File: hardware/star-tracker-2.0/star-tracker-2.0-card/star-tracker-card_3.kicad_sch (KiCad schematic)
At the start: 60 parts, among them J100 DM3BT-DSF-PEJS, U11 TCAN330, U3 EMMC+RESET+5.1-COMPATIBLE-BA, U7 OSD3358-512M-BSM

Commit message: Added IMU
added IMU, and i2c pull up resistors to schematic.
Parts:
- removed TP1, TP2: TEST-POINT3X4, oresat-misc:TestPoint_Pad_D1.0mm, symbol oresat-misc:Test-Point-1mm-round
- added C40: 100n, oresat-passives:0603-C-NOSILK, symbol Device:C_Small
- added C41: 2.2u, oresat-passives:0603-C-NOSILK, symbol Device:C_Small
- added C44: 10n, oresat-passives:0603-C-NOSILK, symbol Device:C_Small
- added R59, R60, R75, R79: 4.7k, oresat-passives:0603-C-NOSILK, symbol Device:R_Small_US
- added U17: ICM-42688-P, oresat-ics:PQFN50P300X250X97-14N, symbol oresat-ics:ICM-42688-P
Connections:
- net 3.3V: now also C40.1, C41.1, C44.1, R59.2, R75.2, R79.2, U17.5 (VDDIO), U17.8 (VDD)
- net GND: now also C40.2, C41.2, C44.2, R60.1, U17.10 (RESV_10), U17.11 (RESV_11), U17.6 (GND), U17.7 (RESV_7)
- net at U7.A13 (SPI0_SCLK): now also R79.1, U17.14 (AP_SDA/AP_SDIO/AP_SDI)
- net at U7.B13 (SPI0_D0): now also R75.1, U17.13 (AP_SCL/AP_SCLK)
- new net: R59.1, U17.12 (AP_CS)
- new net: R60.2, U17.1 (AP_SDO/AP_AD0)
- new net IMU_INT1: U17.4 (INT1/INT)
- new net IMU_INT2: U17.9 (INT2/FSYNC/CLKIN)
- no-connect marks 8 -> 10
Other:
- note added: "IMU (3 ACC + 3 GYRO)"
- moved on the sheet: C10, C11, C12, C2, C3, C31, C5, C6, C8, C9, D2, D3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

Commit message: Routine Push
Updated schematic and layout. about 60% done with routing.
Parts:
- removed R9: 10K Array, star-tracker-card:ARRAY_EXBA-M, symbol star-tracker-card-eagle-import:EXB-A10P391JC_ARRAY_EXBA-M
- removed TP100, TP101, TP103, TP104, TP105, TP106, TP107, TP108, TP111, TP114, TP115, TP117, TP118, TP120, TP122, TP123, TP124, TP125, TP126, TP127, TP128, TP131, TP134, TP14, TP177, TP178, TP180, TP30, TP31: TEST-POINT3X4, oresat-misc:TestPoint_Pad_D1.0mm, symbol oresat-misc:Test-Point-1mm-round
- added R80, R81: 10k, oresat-passives:0603-C-NOSILK, symbol Device:R_Small_US
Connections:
- net 3.3V: now also R80.2, R81.2
- net D1_I: now also R8.1 (11); no longer R8.9 (99)
- net EMMC_CMD: now also R10.6 (66)
- net EMMC_D0: now also R10.8 (88)
- net EMMC_D1: now also R10.4 (44); no longer R10.1 (11)
- net EMMC_D2: now also R80.1; no longer R10.9 (99)
- net EMMC_D3: now also R10.2 (22)
- net EMMC_D4: now also R10.7 (77)
- net EMMC_D5: now also R81.1
- net EMMC_D6: now also R10.9 (99); no longer R10.8 (88)
- net EMMC_D7: now also R10.1 (11); no longer R10.2 (22)
- net EMMC_SCK: now also R10.3 (33)
- net EMMC_nRST: no longer R10.3 (33)
- no-connect marks 10 -> 34

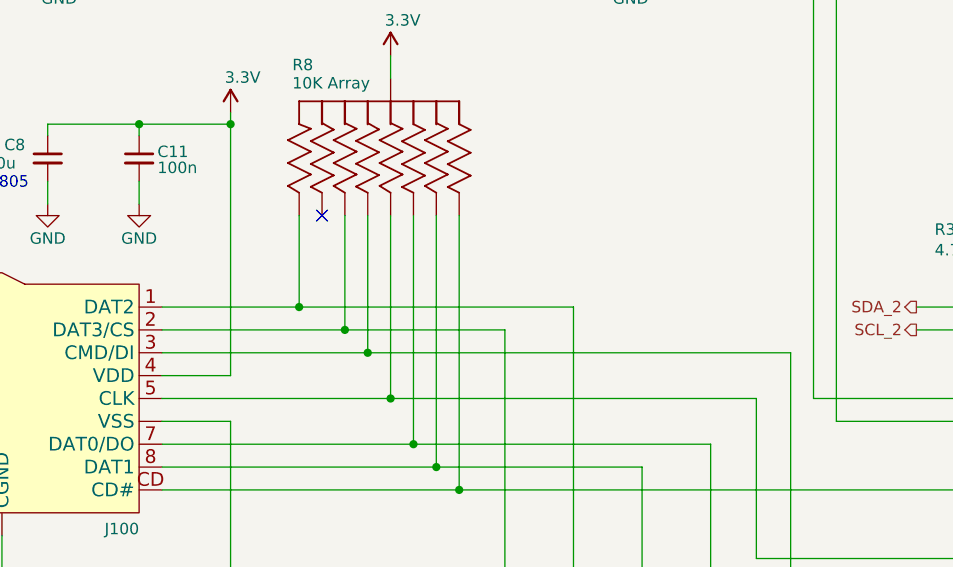
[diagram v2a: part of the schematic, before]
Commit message: Star Tracker 2.0
Layout and routing 100% completed. Only needs minor adjustments for silkscreen and camera mounting holes.
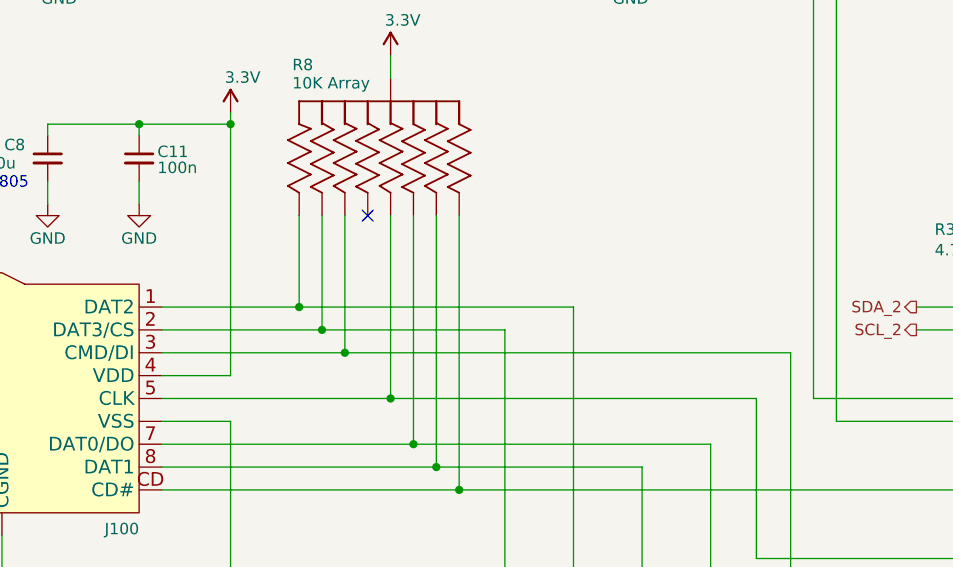
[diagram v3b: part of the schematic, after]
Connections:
- net D0_I: now also R8.9 (99); no longer R8.2 (22)
- net MMC1_CMD: now also R8.2 (22); no longer R8.8 (88)
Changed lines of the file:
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@@
+	)
+	(junction
+		(at 80.01 138.43)
+		(diameter 0)
+		(color 0 0 0 0)
 	)
 	(junction
@@
 	)
 	(junction
-		(at 80.01 135.89)
-		(diameter 0)
-		(color 0 0 0 0)
-	)
-	(junction
 		(at 41.91 163.83)
 		(diameter 0)
@@
 	)
 	(junction
+		(at 77.47 135.89)
+		(diameter 0)
+		(color 0 0 0 0)
+	)
+	(junction
 		(at 400.05 166.37)
 		(diameter 0)
@@
 	)
 	(junction
-		(at 82.55 138.43)
-		(diameter 0)
-		(color 0 0 0 0)
-	)
-	(junction
 		(at 361.95 152.4)
 		(diameter 0)
@@
 	)
 	(no_connect
-		(at 77.47 123.19)
-	)
-	(no_connect
 		(at 52.07 77.47)
 	)
 	(no_connect
+		(at 82.55 123.19)
+	)
+	(no_connect
 		(at 186.69 151.13)
 	)
@@
 	(wire
 		(pts
-			(xy 82.55 138.43) (xy 129.54 138.43)
+			(xy 80.01 138.43) (xy 129.54 138.43)
 		)
 		(stroke
@@
 	(wire
 		(pts
+			(xy 77.47 123.19) (xy 77.47 135.89)
+		)
+		(stroke
+			(width 0)
+			(type default)
+		)
+	)
+	(wire
+		(pts
 			(xy 217.17 58.42) (xy 217.17 57.15)
 		)
@@
 	(wire
 		(pts
-			(xy 59.69 135.89) (xy 80.01 135.89)
-		)
-		(stroke
-			(width 0.1524)
-			(type solid)
-		)
-	)
-	(wire
-		(pts
 			(xy 102.87 77.47) (xy 134.62 77.47)
 		)
@@
 	(wire
 		(pts
-			(xy 97.79 135.89) (xy 80.01 135.89)
+			(xy 59.69 135.89) (xy 77.47 135.89)
 		)
 		(stroke
@@
 	(wire
 		(pts
-			(xy 59.69 138.43) (xy 82.55 138.43)
+			(xy 59.69 138.43) (xy 80.01 138.43)
 		)
 		(stroke
@@
 	(wire
 		(pts
+			(xy 77.47 135.89) (xy 97.79 135.89)
+		)
+		(stroke
+			(width 0.1524)
+			(type solid)
+		)
+	)
+	(wire
+		(pts
 			(xy 247.65 173.99) (xy 311.15 173.99)
 		)
@@
 	(wire
 		(pts
+			(xy 80.01 123.19) (xy 80.01 138.43)
+		)
+		(stroke
+			(width 0)
+			(type default)
+		)
+	)
+	(wire
+		(pts
 			(xy 292.1 149.86) (xy 292.1 152.4)
 		)
@@
 	(wire
 		(pts
-			(xy 80.01 135.89) (xy 80.01 123.19)
-		)
-		(stroke
-			(width 0.1524)
-			(type solid)
-		)
-	)
-	(wire
-		(pts
 			(xy 265.43 120.65) (xy 283.21 120.65)
 		)
@@
 		)
 	)
-	(wire
-		(pts
-			(xy 82.55 138.43) (xy 82.55 123.19)
-		)
-		(stroke
-			(width 0.1524)
-			(type solid)
-		)
-	)

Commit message: Star tracker board update
Added 3d models to footprints, reannotated component designators
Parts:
- U7: footprint star-tracker-card:OSD335X-BGA-256 -> oresat-ics:U-Octavo-OSD335X-BGA-256; symbol star-tracker-card-eagle-import:OSD3358-512M-BSM -> oresat-ics:OSD3358-512M-BSM; Distributor (none) -> DigiKey; MPN OSD3358-1G-ISM -> OSD3358-512M-BSM
- renumbered C44 to C30, C41 to C31, C40 to C32, C8 to C33, C11 to C34, C31 to C35, C12 to C36, C10 to C37, C9 to C38, C6 to C39, C5 to C40, C3 to C41, C2 to C42, D2 to D5, D3 to D6, D4 to D7, D5 to D8, J100 to J5, R8 to R57, R60 to R58, R79 to R60, R75 to R61, R30 to R62, R29 to R63, R2 to R64, R3 to R65, R4 to R66, R5 to R67, R80 to R68, R81 to R69, R10 to R70, TP142 to TP23, TP146 to TP24, U17 to U11, U11 to U12, U3 to U13

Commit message: Component linking
Linked components to 3d models
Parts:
- C33, C42: DPN 490-GRT21BC71E106KE13KCT-ND -> 1276-CL21B106KAYQNNETR-ND; MFR Murata Electronics -> Samsung Electro-Mechanics; MPN GRT21BC71E106KE13K -> CL21B106KAYQNNE
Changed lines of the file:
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@@
 			)
 		)
-		(property "Datasheet" "https://search.murata.co.jp/Ceramy/image/img/A01X/G101/ENG/GRT21BC71E106KE13-01.pdf"
+		(property "Datasheet" "https://mm.digikey.com/Volume0/opasdata/d220001/medias/docus/7851/1276_CL21B1.pdf"
 			(at 407.67 156.21 0)
 			(hide yes)
@@
 			)
 		)
-		(property "Description" "10 µF ±10% 25V Ceramic Capacitor X7S 0805 (2012 Metric)"
+		(property "Description" "10 µF ±10% 25V Ceramic Capacitor X7R 0805 (2012 Metric)"
 			(at 407.67 156.21 0)
 			(hide yes)
@@
 			)
 		)
-		(property "DPN" "490-GRT21BC71E106KE13KCT-ND"
+		(property "DPN" "1276-CL21B106KAYQNNETR-ND"
 			(at 407.67 156.21 0)
 			(hide yes)
@@
 			)
 		)
-		(property "MFR" "Murata Electronics"
+		(property "MFR" "Samsung Electro-Mechanics"
 			(at 407.67 156.21 0)
 			(hide yes)
@@
 			)
 		)
-		(property "MPN" "GRT21BC71E106KE13K"
+		(property "MPN" "CL21B106KAYQNNE"
 			(at 407.67 156.21 0)
 			(hide yes)
@@
 			)
 		)
-		(property "Datasheet" "https://search.murata.co.jp/Ceramy/image/img/A01X/G101/ENG/GRT21BC71E106KE13-01.pdf"
+		(property "Datasheet" "https://mm.digikey.com/Volume0/opasdata/d220001/medias/docus/7851/1276_CL21B1.pdf"
 			(at 46.99 116.84 0)
 			(hide yes)
@@
 			)
 		)
-		(property "Description" "10 µF ±10% 25V Ceramic Capacitor X7S 0805 (2012 Metric)"
+		(property "Description" "10 µF ±10% 25V Ceramic Capacitor X7R 0805 (2012 Metric)"
 			(at 46.99 116.84 0)
 			(hide yes)
@@
 			)
 		)
-		(property "DPN" "490-GRT21BC71E106KE13KCT-ND"
+		(property "DPN" "1276-CL21B106KAYQNNETR-ND"
 			(at 46.99 116.84 0)
 			(hide yes)
@@
 			)
 		)
-		(property "MFR" "Murata Electronics"
+		(property "MFR" "Samsung Electro-Mechanics"
 			(at 46.99 116.84 0)
 			(hide yes)
@@
 			)
 		)
-		(property "MPN" "GRT21BC71E106KE13K"
+		(property "MPN" "CL21B106KAYQNNE"
 			(at 46.99 116.84 0)
 			(hide yes)

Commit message: Added extra Testpoints
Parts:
- added TP55, TP56: Test-Point, oresat-misc:TestPoint_Pad_D1.0mm, symbol oresat-misc:Test-Point-1mm-round
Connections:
- net at R60.1, U11.14 (AP_SDA/AP_SDIO/AP_SDI), U7.A13 (SPI0_SCLK): now also TP56.1
- net at R61.1, U11.13 (AP_SCL/AP_SCLK), U7.B13 (SPI0_D0): now also TP55.1
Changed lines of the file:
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@@
 	)
 	(junction
+		(at 132.08 93.98)
+		(diameter 0)
+		(color 0 0 0 0)
+	)
+	(junction
 		(at 151.13 123.19)
 		(diameter 0)
@@
 	)
 	(junction
+		(at 134.62 97.79)
+		(diameter 0)
+		(color 0 0 0 0)
+	)
+	(junction
 		(at 292.1 179.07)
 		(diameter 0)
@@
 	(wire
 		(pts
+			(xy 132.08 93.98) (xy 132.08 80.01)
+		)
+		(stroke
+			(width 0.1524)
+			(type solid)
+		)
+	)
+	(wire
+		(pts
 			(xy 102.87 82.55) (xy 111.76 82.55)
 		)
@@
 	(wire
 		(pts
+			(xy 102.87 69.85) (xy 110.49 69.85)
+		)
+		(stroke
+			(width 0)
+			(type default)
+		)
+	)
+	(wire
+		(pts
 			(xy 158.75 123.19) (xy 158.75 124.46)
 		)
@@
 	(wire
 		(pts
+			(xy 41.91 69.85) (xy 52.07 69.85)
+		)
+		(stroke
+			(width 0)
+			(type default)
+		)
+	)
+	(wire
+		(pts
 			(xy 334.01 201.93) (xy 323.85 201.93)
 		)
@@
 	(wire
 		(pts
-			(xy 132.08 143.51) (xy 132.08 80.01)
+			(xy 132.08 143.51) (xy 132.08 93.98)
 		)
 		(stroke
@@
 	(wire
 		(pts
+			(xy 134.62 97.79) (xy 134.62 77.47)
+		)
+		(stroke
+			(width 0.1524)
+			(type solid)
+		)
+	)
+	(wire
+		(pts
 			(xy 400.05 153.67) (xy 400.05 148.59)
 		)
@@
 	(wire
 		(pts
-			(xy 106.68 69.85) (xy 102.87 69.85)
-		)
-		(stroke
-			(width 0)
-			(type default)
-		)
-	)
-	(wire
-		(pts
 			(xy 265.43 135.89) (xy 265.43 120.65)
 		)
@@
 	(wire
 		(pts
-			(xy 134.62 146.05) (xy 134.62 77.47)
+			(xy 134.62 146.05) (xy 134.62 97.79)
 		)
 		(stroke
@@
 	(wire
 		(pts
-			(xy 52.07 69.85) (xy 48.26 69.85)
-		)
-		(stroke
-			(width 0)
-			(type default)
-		)
-	)
-	(wire
-		(pts
 			(xy 384.81 166.37) (xy 384.81 161.29)
 		)
@@
 	(hierarchical_label "IMU_INT1"
 		(shape output)
-		(at 48.26 69.85 180)
+		(at 41.91 69.85 180)
 		(effects
 			(font
@@
 	(hierarchical_label "IMU_INT2"
 		(shape output)
-		(at 106.68 69.85 0)
+		(at 110.49 69.85 0)
 		(effects
 			(font
@@
 	)
 	(symbol
+		(lib_id "oresat-misc:Test-Point-1mm-round")
+		(at 134.62 97.79 0)
+		(mirror y)
+		(unit 1)
+		(body_style 1)
+		(exclude_from_sim yes)
+		(in_bom no)
+		(on_board yes)
+		(in_pos_files yes)
+		(dnp no)
+		(property "Reference" "TP55"
+			(at 140.97 97.79 0)
+			(show_name no)
+			(do_not_autoplace no)
+			(effects
+				(font
+					(size 1.27 1.27)
+				)
+				(justify left)
+			)
+		)
+		(property "Value" "Test-Point"
+			(at 134.62 95.25 0)
+			(hide yes)
+			(show_name no)
+			(do_not_autoplace no)
+			(effects
+				(font
+					(size 1.27 1.27)
+				)
+			)
+		)
+		(property "Footprint" "oresat-misc:TestPoint_Pad_D1.0mm"
+			(at 134.62 87.63 0)
+			(hide yes)
+			(show_name no)
+			(do_not_autoplace no)
+			(effects
+				(font
+					(size 1.27 1.27)
+				)
+			)
+		)
+		(property "Datasheet" ""
+			(at 134.62 97.79 0)
+			(hide yes)
+			(show_name no)
+			(do_not_autoplace no)
+			(effects
+				(font
+					(size 1.27 1.27)
+				)
+			)
+		)
+		(property "Description" "1mm round SMT test point"
+			(at 134.62 97.79 0)
+			(hide yes)
+			(show_name no)
+			(do_not_autoplace no)
+			(effects
+				(font
+					(size 1.27 1.27)
+				)
+			)
+		)
+		(pin "1"
+		)
+		(instances
+			(project "star-tracker-card"
+				(path "/324e9eb5-7420-4b7e-862c-cc20bb28618a/c38dcfbe-e8e3-410e-98db-09d235320446"
+					(reference "TP55")
+					(unit 1)
+				)
+			)
+		)
+	)
+	(symbol
 		(lib_id "Device:C_Small")
 		(at 369.57 156.21 0)
@@
 					(unit 1)
 				)
+			)
+		)
+	)
+	(symbol
+		(lib_id "oresat-misc:Test-Point-1mm-round")
+		(at 132.08 93.98 0)
+		(mirror x)
+		(unit 1)
+		(body_style 1)
+		(exclude_from_sim yes)
+		(in_bom no)
+		(on_board yes)
+		(in_pos_files yes)
+		(dnp no)
+		(property "Reference" "TP56"
+			(at 125.73 93.98 0)
+			(show_name no)
+			(do_not_autoplace no)
+			(effects
+				(font
+					(size 1.27 1.27)
+				)
+				(justify left)
+			)
+		)
+		(property "Value" "Test-Point"
+			(at 132.08 96.52 0)
+			(hide yes)
+			(show_name no)
+			(do_not_autoplace no)
+			(effects
+				(font
+					(size 1.27 1.27)
+				)
+			)
+		)
+		(property "Footprint" "oresat-misc:TestPoint_Pad_D1.0mm"
+			(at 132.08 104.14 0)
+			(hide yes)
+			(show_name no)
+			(do_not_autoplace no)
+			(effects
+				(font
+					(size 1.27 1.27)
+				)
+			)
+		)
+		(property "Datasheet" ""
+			(at 132.08 93.98 0)
+			(hide yes)
+			(show_name no)
+			(do_not_autoplace no)
+			(effects
+				(font
+					(size 1.27 1.27)
+				)
+			)
+		)
+		(property "Description" "1mm round SMT test point"
+			(at 132.08 93.98 0)
+			(hide yes)
+			(show_name no)
+			(do_not_autoplace no)
+			(effects
+				(font
+					(size 1.27 1.27)
+				)
+			)
+		)
+		(pin "1"
+		)
+		(instances
+			(project "star-tracker-card"
+				(path "/324e9eb5-7420-4b7e-862c-cc20bb28618a/c38dcfbe-e8e3-410e-98db-09d235320446"
+					(reference "TP56")
+					(unit 1)
+				)
